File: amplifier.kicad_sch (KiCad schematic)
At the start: 14 parts, among them J1 Mic Connector, J2 Gain Jumper, J3 BIAS Jumper, U1 MAX9814, U2 MIC5365-3.0YD5

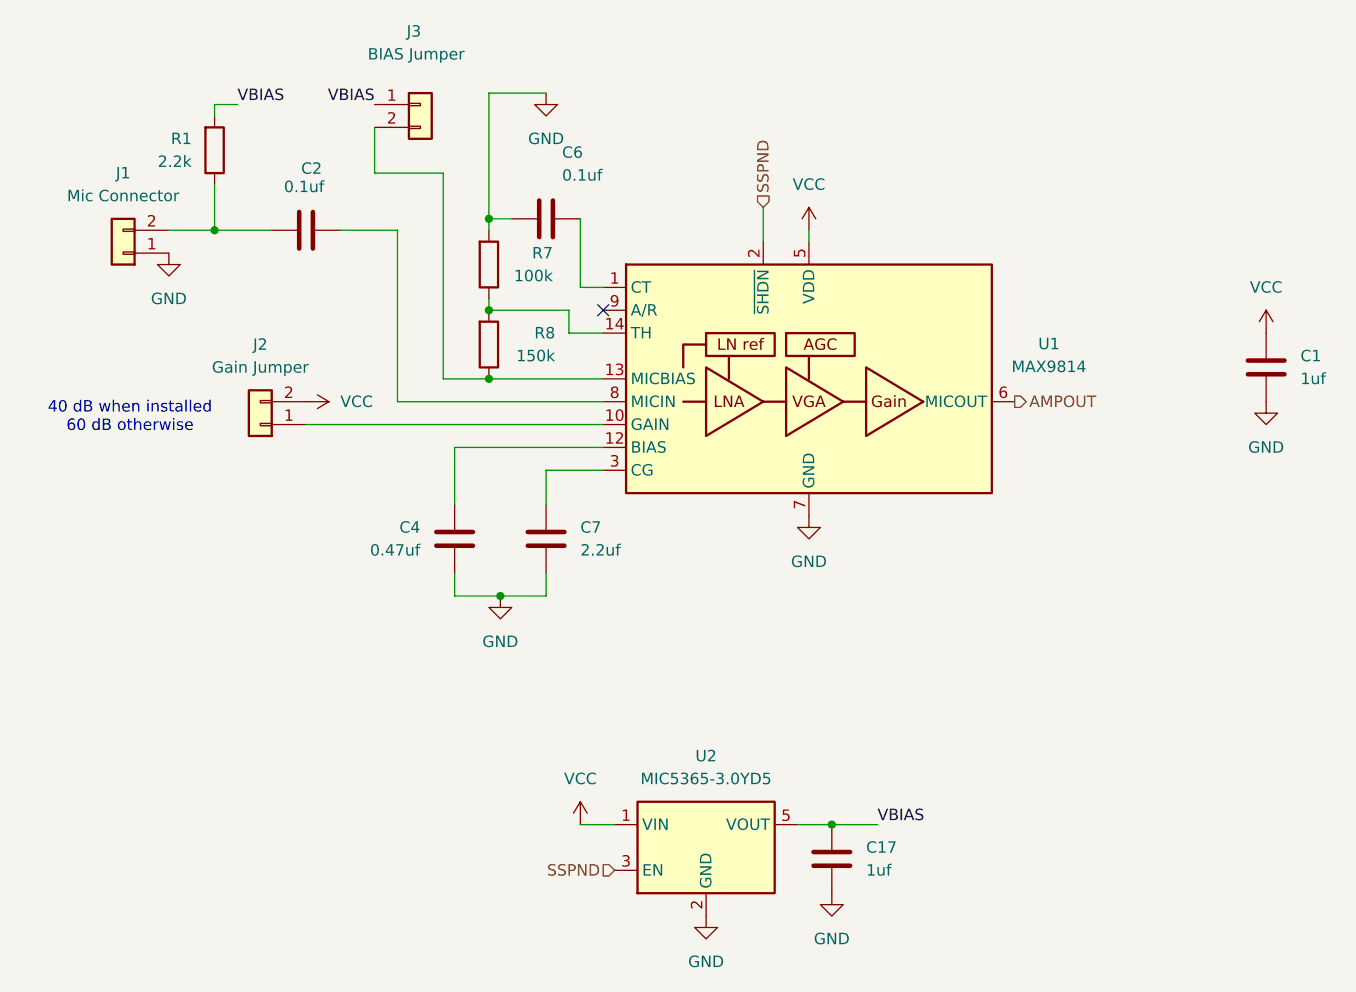
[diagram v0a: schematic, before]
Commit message: Add `Power`, `Connectors` and `Codec`
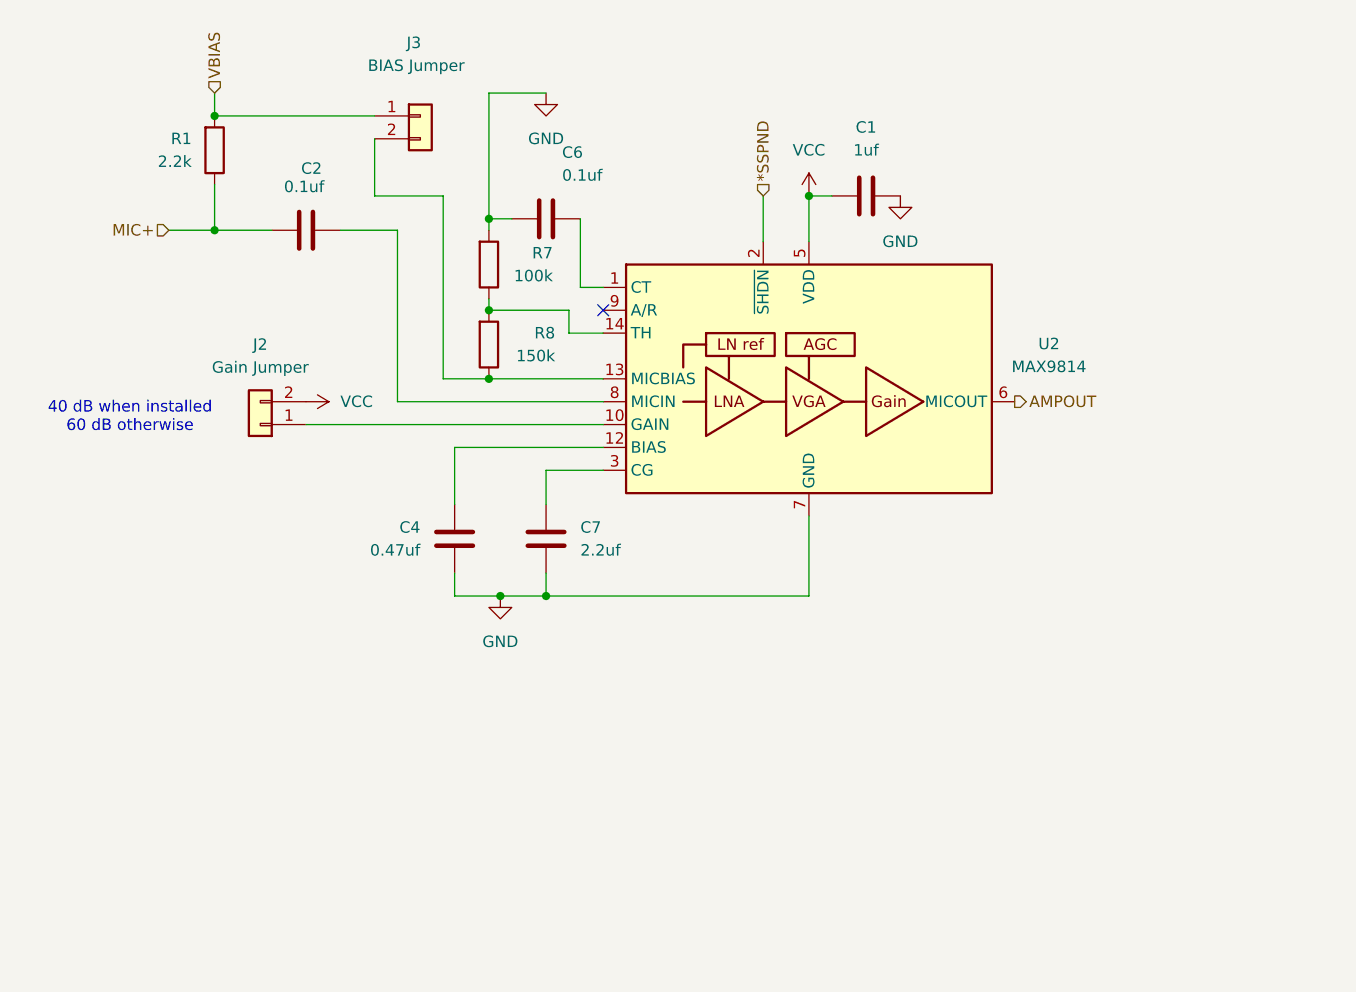
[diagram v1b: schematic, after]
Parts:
- removed C17: 1uf, symbol Device:C
- removed J1: Mic Connector, symbol Connector_Generic:Conn_01x02
- removed U2: MIC5365-3.0YD5, Package_TO_SOT_SMD:TSOT-23-5, symbol Regulator_Linear:MIC5365-3.3YD5
- renumbered U1 to U2
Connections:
- net MIC+: now reaches C2.2, R1.1
- net SSPND renamed *SSPND
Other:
- company: (none) -> Vladyslav Kukharchuk <vladyslavziuziun@gmail.com>
- moved on the sheet: C1, J3

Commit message: Assign Footprints
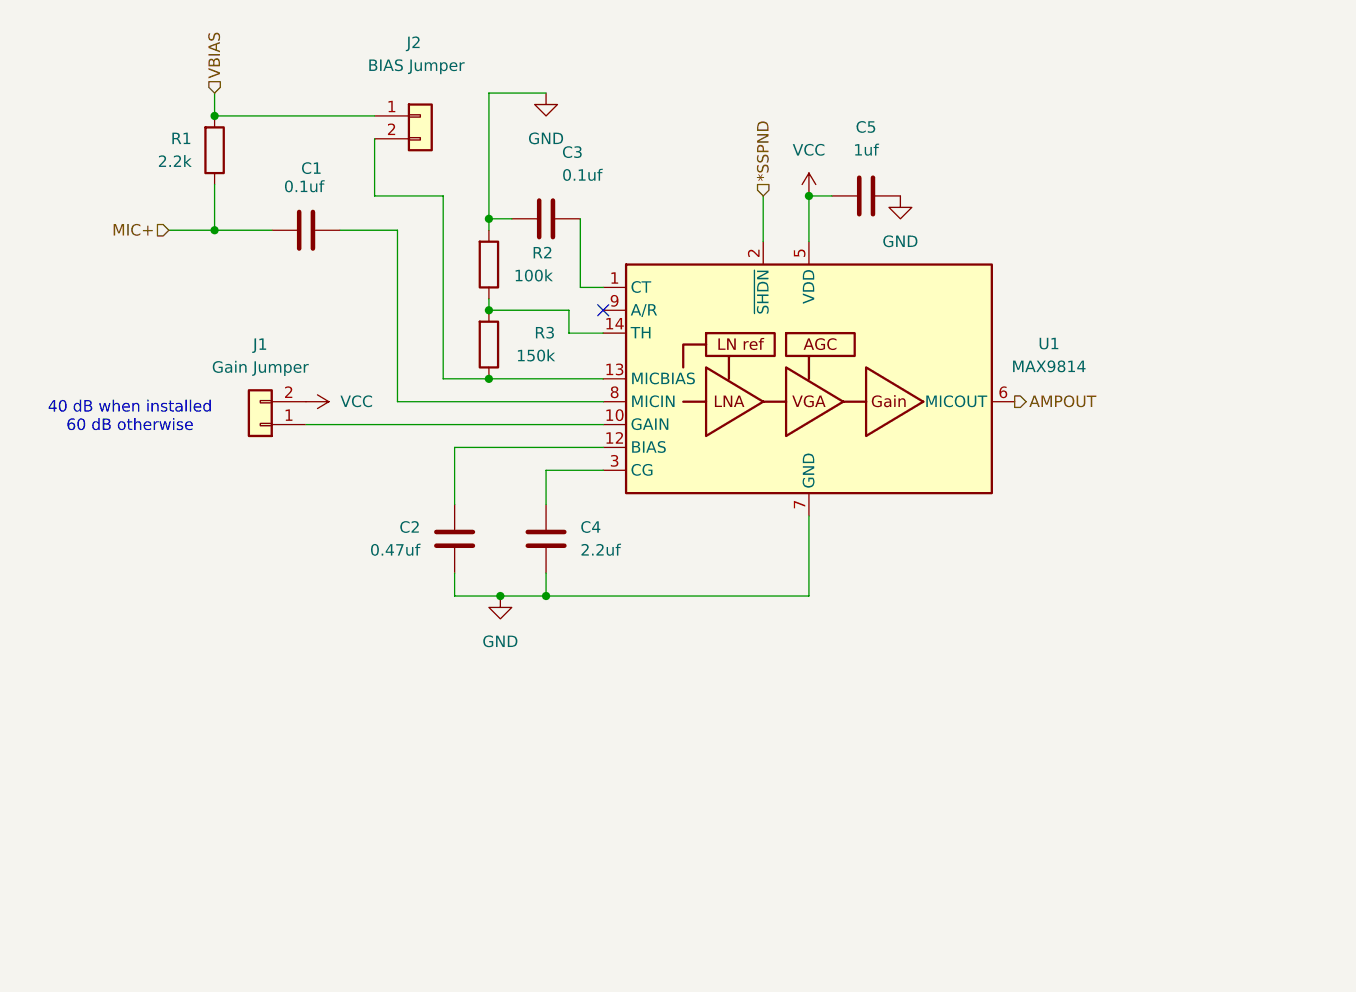
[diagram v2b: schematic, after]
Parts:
- C1: renamed from C2; footprint (none) -> Capacitor_SMD:C_0603_1608Metric_Pad1.08x0.95mm_HandSolder
- C2: renamed from C4; footprint (none) -> Capacitor_SMD:C_0603_1608Metric_Pad1.08x0.95mm_HandSolder
- C3: renamed from C6; footprint (none) -> Capacitor_SMD:C_0603_1608Metric_Pad1.08x0.95mm_HandSolder
- C4: renamed from C7; footprint (none) -> Capacitor_SMD:C_0603_1608Metric_Pad1.08x0.95mm_HandSolder
- C5: renamed from C1; footprint (none) -> Capacitor_SMD:C_0603_1608Metric_Pad1.08x0.95mm_HandSolder
- J1: renamed from J2; footprint (none) -> Connector_PinHeader_1.27mm:PinHeader_1x02_P1.27mm_Vertical
- J2: renamed from J3; footprint (none) -> Connector_PinHeader_1.27mm:PinHeader_1x02_P1.27mm_Vertical
- R1: footprint (none) -> Resistor_SMD:R_0603_1608Metric_Pad0.98x0.95mm_HandSolder
- R2: renamed from R7; footprint (none) -> Resistor_SMD:R_0603_1608Metric_Pad0.98x0.95mm_HandSolder
- R3: renamed from R8; footprint (none) -> Resistor_SMD:R_0603_1608Metric_Pad0.98x0.95mm_HandSolder
- renumbered U2 to U1
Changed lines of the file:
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@@
 		(dnp no)
 		(fields_autoplaced yes)
-		(property "Reference" "C1"
+		(property "Reference" "C5"
 			(at 170.18 55.88 90)
 			(effects
@@
 			)
 		)
-		(property "Footprint" ""
+		(property "Footprint" "Capacitor_SMD:C_0603_1608Metric_Pad1.08x0.95mm_HandSolder"
 			(at 173.99 62.5348 0)
 			(effects
@@
 			(project "Microphone"
 				(path "/dc202712-23ff-46da-8ec2-2a828c683a4d/e395ea73-b08d-4ba3-8b06-fa01b208b024"
-					(reference "C1")
+					(reference "C5")
 					(unit 1)
 				)
@@
 		(dnp no)
 		(fields_autoplaced yes)
-		(property "Reference" "#PWR08"
+		(property "Reference" "#PWR03"
 			(at 134.62 58.42 0)
 			(effects
@@
 			(project "Microphone"
 				(path "/dc202712-23ff-46da-8ec2-2a828c683a4d/e395ea73-b08d-4ba3-8b06-fa01b208b024"
-					(reference "#PWR08")
+					(reference "#PWR03")
 					(unit 1)
 				)
@@
 		(on_board yes)
 		(dnp no)
-		(property "Reference" "C4"
+		(property "Reference" "C2"
 			(at 120.65 100.3299 0)
 			(effects
@@
 			)
 		)
-		(property "Footprint" ""
+		(property "Footprint" "Capacitor_SMD:C_0603_1608Metric_Pad1.08x0.95mm_HandSolder"
 			(at 123.4948 105.41 0)
 			(effects
@@
 			(project "Microphone"
 				(path "/dc202712-23ff-46da-8ec2-2a828c683a4d/e395ea73-b08d-4ba3-8b06-fa01b208b024"
-					(reference "C4")
+					(reference "C2")
 					(unit 1)
 				)
@@
 		(dnp no)
 		(fields_autoplaced yes)
-		(property "Reference" "J2"
+		(property "Reference" "J1"
 			(at 102.87 80.01 0)
 			(effects
@@
 			)
 		)
-		(property "Footprint" ""
+		(property "Footprint" "Connector_PinHeader_1.27mm:PinHeader_1x02_P1.27mm_Vertical"
 			(at 102.87 88.9 0)
 			(effects
@@
 			(project ""
 				(path "/dc202712-23ff-46da-8ec2-2a828c683a4d/e395ea73-b08d-4ba3-8b06-fa01b208b024"
-					(reference "J2")
+					(reference "J1")
 					(unit 1)
 				)
@@
 		(dnp no)
 		(fields_autoplaced yes)
-		(property "Reference" "#PWR02"
+		(property "Reference" "#PWR05"
 			(at 173.99 69.85 0)
 			(effects
@@
 			(project ""
 				(path "/dc202712-23ff-46da-8ec2-2a828c683a4d/e395ea73-b08d-4ba3-8b06-fa01b208b024"
-					(reference "#PWR02")
+					(reference "#PWR05")
 					(unit 1)
 				)
@@
 			)
 		)
-		(property "Footprint" ""
+		(property "Footprint" "Resistor_SMD:R_0603_1608Metric_Pad0.98x0.95mm_HandSolder"
 			(at 96.012 58.42 90)
 			(effects
@@
 		(dnp no)
 		(fields_autoplaced yes)
-		(property "Reference" "#PWR05"
+		(property "Reference" "#PWR02"
 			(at 129.54 114.3 0)
 			(effects
@@
 			(project "Microphone"
 				(path "/dc202712-23ff-46da-8ec2-2a828c683a4d/e395ea73-b08d-4ba3-8b06-fa01b208b024"
-					(reference "#PWR05")
+					(reference "#PWR02")
 					(unit 1)
 				)
@@
 		(dnp no)
 		(fields_autoplaced yes)
-		(property "Reference" "#PWR06"
+		(property "Reference" "#PWR01"
 			(at 104.14 86.36 0)
 			(effects
@@
 			(project "Microphone"
 				(path "/dc202712-23ff-46da-8ec2-2a828c683a4d/e395ea73-b08d-4ba3-8b06-fa01b208b024"
-					(reference "#PWR06")
+					(reference "#PWR01")
 					(unit 1)
 				)
@@
 		(on_board yes)
 		(dnp no)
-		(property "Reference" "J3"
+		(property "Reference" "J2"
 			(at 119.126 46.482 0)
 			(effects
@@
 			)
 		)
-		(property "Footprint" ""
+		(property "Footprint" "Connector_PinHeader_1.27mm:PinHeader_1x02_P1.27mm_Vertical"
 			(at 120.65 54.61 0)
 			(effects
@@
 			(project "Microphone"
 				(path "/dc202712-23ff-46da-8ec2-2a828c683a4d/e395ea73-b08d-4ba3-8b06-fa01b208b024"
-					(reference "J3")
+					(reference "J2")
 					(unit 1)
 				)
@@
 		(dnp no)
 		(fields_autoplaced yes)
-		(property "Reference" "C7"
+		(property "Reference" "C4"
 			(at 138.43 100.3299 0)
 			(effects
@@
 			)
 		)
-		(property "Footprint" ""
+		(property "Footprint" "Capacitor_SMD:C_0603_1608Metric_Pad1.08x0.95mm_HandSolder"
 			(at 135.5852 105.41 0)
 			(effects
@@
 			(project "Microphone"
 				(path "/dc202712-23ff-46da-8ec2-2a828c683a4d/e395ea73-b08d-4ba3-8b06-fa01b208b024"
-					(reference "C7")
+					(reference "C4")
 					(unit 1)
 				)
@@
 		(dnp no)
 		(fields_autoplaced yes)
-		(property "Reference" "U2"
+		(property "Reference" "U1"
 			(at 190.5 79.9398 0)
 			(effects
@@
 			(project ""
 				(path "/dc202712-23ff-46da-8ec2-2a828c683a4d/e395ea73-b08d-4ba3-8b06-fa01b208b024"
-					(reference "U2")
+					(reference "U1")
 					(unit 1)
 				)
@@
 		(on_board yes)
 		(dnp no)
-		(property "Reference" "C2"
+		(property "Reference" "C1"
 			(at 109.728 60.452 90)
 			(effects
@@
 			)
 		)
-		(property "Footprint" ""
+		(property "Footprint" "Capacitor_SMD:C_0603_1608Metric_Pad1.08x0.95mm_HandSolder"
 			(at 104.14 66.3448 0)
 			(effects
@@
 			(project "Microphone"
 				(path "/dc202712-23ff-46da-8ec2-2a828c683a4d/e395ea73-b08d-4ba3-8b06-fa01b208b024"
-					(reference "C2")
+					(reference "C1")
 					(unit 1)
 				)
@@
 		(dnp no)
 		(fields_autoplaced yes)
-		(property "Reference" "#PWR03"
+		(property "Reference" "#PWR04"
 			(at 163.83 67.31 0)
 			(effects
@@
 			(project "Microphone"
 				(path "/dc202712-23ff-46da-8ec2-2a828c683a4d/e395ea73-b08d-4ba3-8b06-fa01b208b024"
-					(reference "#PWR03")
+					(reference "#PWR04")
 					(unit 1)
 				)
@@
 		(on_board yes)
 		(dnp no)
-		(property "Reference" "R7"
+		(property "Reference" "R2"
 			(at 135.382 69.85 0)
 			(effects
@@
 			)
 		)
-		(property "Footprint" ""
+		(property "Footprint" "Resistor_SMD:R_0603_1608Metric_Pad0.98x0.95mm_HandSolder"
 			(at 126.492 71.12 90)
 			(effects
@@
 			(project "Microphone"
 				(path "/dc202712-23ff-46da-8ec2-2a828c683a4d/e395ea73-b08d-4ba3-8b06-fa01b208b024"
-					(reference "R7")
+					(reference "R2")
 					(unit 1)
 				)
@@
 		(on_board yes)
 		(dnp no)
-		(property "Reference" "C6"
+		(property "Reference" "C3"
 			(at 136.398 58.674 90)
 			(effects
@@
 			)
 		)
-		(property "Footprint" ""
+		(property "Footprint" "Capacitor_SMD:C_0603_1608Metric_Pad1.08x0.95mm_HandSolder"
 			(at 138.43 65.0748 0)
 			(effects
@@
 			(project "Microphone"
 				(path "/dc202712-23ff-46da-8ec2-2a828c683a4d/e395ea73-b08d-4ba3-8b06-fa01b208b024"
-					(reference "C6")
+					(reference "C3")
 					(unit 1)
 				)
@@
 		(on_board yes)
 		(dnp no)
-		(property "Reference" "R8"
+		(property "Reference" "R3"
 			(at 135.636 78.74 0)
 			(effects
@@
 			)
 		)
-		(property "Footprint" ""
+		(property "Footprint" "Resistor_SMD:R_0603_1608Metric_Pad0.98x0.95mm_HandSolder"
 			(at 126.492 80.01 90)
 			(effects
@@
 			(project "Microphone"
 				(path "/dc202712-23ff-46da-8ec2-2a828c683a4d/e395ea73-b08d-4ba3-8b06-fa01b208b024"
-					(reference "R8")
-					(unit 1)
-				)
+					(reference "R3")
+					(unit 1)
+				)
